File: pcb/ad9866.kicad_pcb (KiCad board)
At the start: 4 copper layers, 48.8 x 51 mm, 71 parts, among them CN1 MEC6-140_CONNECTOR_BEMICRO, CN2 PCIE, P1 CONN_4, P10 CONN_1, P13 CONN_1, P14 CONN_1, P15 Si510 73.728, P16 CONN_3X2, P17 CONN_4, P18 CONN_1, P19 CONN_1, P2 CONN_1, P20 CONN_1, P22 CONN_1, P23 CONN_5, P24 CONN_5, P25 CONN_5, P3 CONN_1, P4 CONN_1, P5 CONN_1, P6 CONN_1, P8 CONN_1, P9 CONN_1, T1 TRANSF_ADT8, T2 TRANSF_ADT2, T3 TRANSF_ADT2, U1 AD9866BCPZ, U2 NCP1117ST33T3G, U3 NCP1117ST33T3G

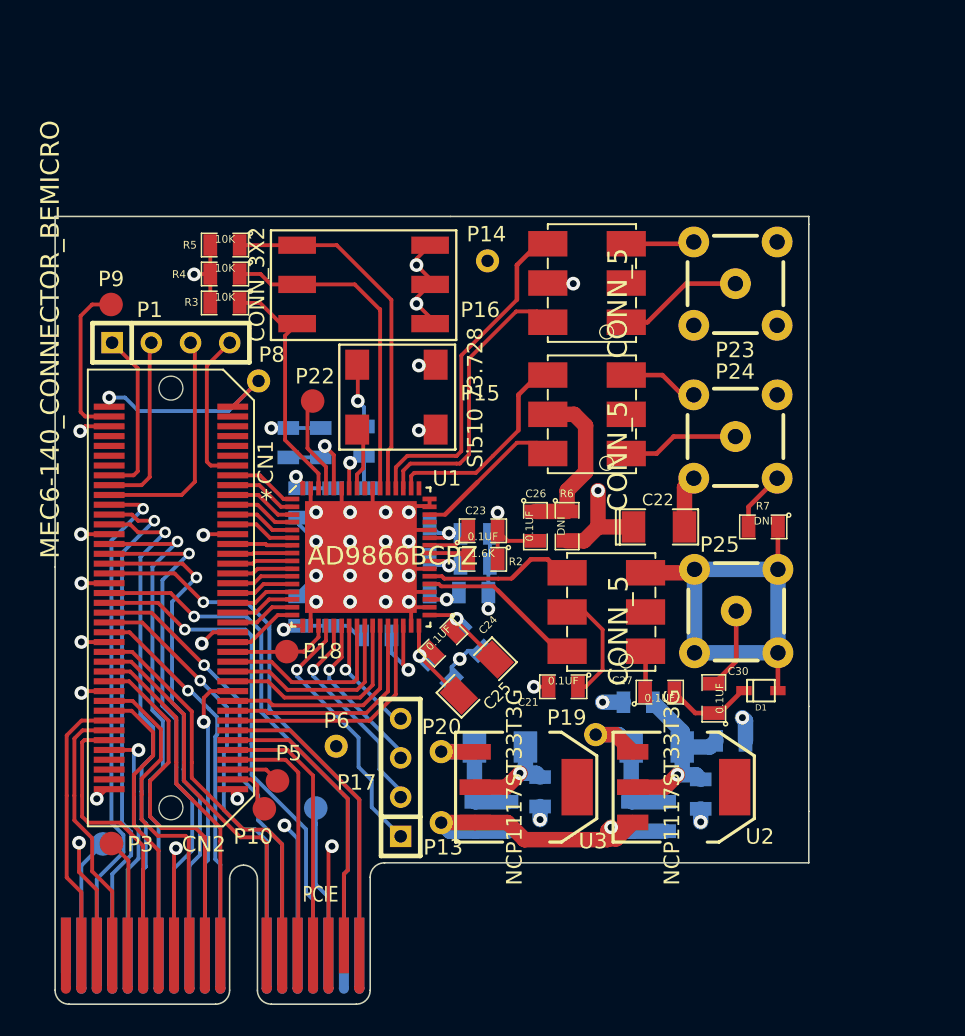
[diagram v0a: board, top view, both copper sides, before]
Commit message: Think 12 is fixed; routed by hand all changes.
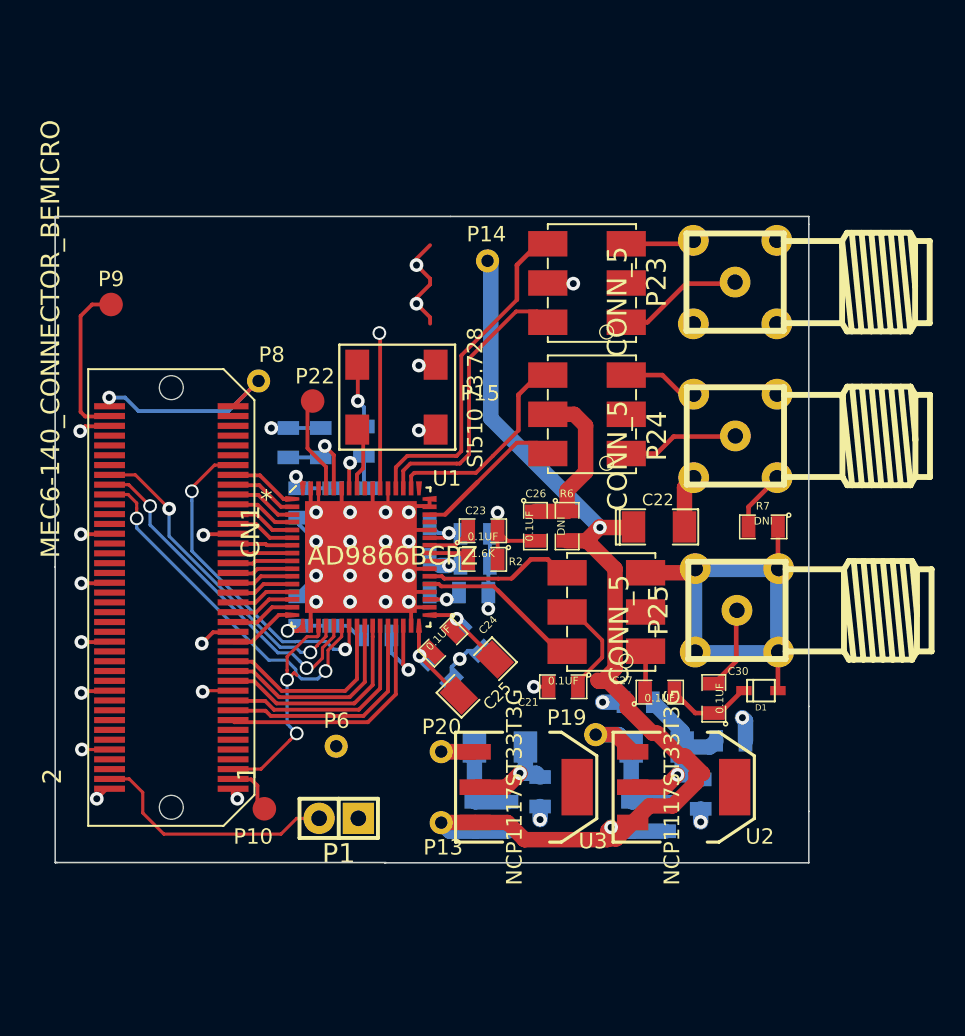
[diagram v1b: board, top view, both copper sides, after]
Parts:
- removed CN2: PCIE, Connect:PCI-EXPRESS
- removed P16: CONN_3X2, DIPSWITCH:DIPSWITCH
- removed P17: CONN_4, Connect:SIL-4
- removed P18, P2, P3, P4, P5: CONN_1, Measurement_Points:Measurement_Point_Round-SMD-Pad_Small
- removed R3, R4, R5: 10K, SMD_Packages:SM0805
- P1: value CONN_4 -> CONN_2; footprint Connect:SIL-4 -> Pin_Headers:Pin_Header_Straight_1x02
- P23, P24, P25: footprint BEMICRO:SMA -> SMA:SMA
- moved P1 32.7 mm to (119.1, 122.4), turned to 180 degrees
- moved P23 0.10 mm to (144.7, 87.7)
- moved P25 0.07 mm to (144.8, 109.0)
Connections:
- CN1 pad 11: Net-(CN1-Pad11) -> (no net)
- CN1 pad 12: Net-(CN1-Pad12) -> (no net)
- CN1 pad 13: Net-(CN1-Pad13) -> (no net)
- CN1 pad 14: Net-(CN1-Pad14) -> (no net)
- CN1 pad 16: Net-(CN1-Pad16) -> (no net)
- CN1 pad 18: Net-(CN1-Pad18) -> (no net)
- CN1 pad 20: Net-(CN1-Pad20) -> (no net)
- CN1 pad 24: Net-(CN1-Pad24) -> (no net)
- CN1 pad 26: Net-(CN1-Pad26) -> (no net)
- CN1 pad 28: Net-(CN1-Pad28) -> (no net)
- CN1 pad 29: Net-(CN1-Pad29) -> (no net)
- CN1 pad 30: Net-(CN1-Pad30) -> (no net)
- CN1 pad 34: Net-(CN1-Pad34) -> (no net)
- CN1 pad 36: Net-(CN1-Pad36) -> (no net)
- CN1 pad 38: Net-(CN1-Pad38) -> (no net)
- CN1 pad 40: Net-(CN1-Pad40) -> (no net)
- CN1 pad 42: Net-(CN1-Pad42) -> (no net)
- CN1 pad 46: Net-(CN1-Pad46) -> (no net)
- CN1 pad 48: Net-(CN1-Pad48) -> (no net)
- CN1 pad 5: Net-(CN1-Pad5) -> /CLKOUT1
- CN1 pad 50: Net-(CN1-Pad50) -> (no net)
- CN1 pad 52: Net-(CN1-Pad52) -> (no net)
- CN1 pad 56: Net-(CN1-Pad56) -> (no net)
- CN1 pad 58: Net-(CN1-Pad58) -> (no net)
- CN1 pad 6: Net-(CN1-Pad6) -> (no net)
- CN1 pad 60: Net-(CN1-Pad60) -> (no net)
- CN1 pad 62: Net-(CN1-Pad62) -> SCLK
- CN1 pad 64: Net-(CN1-Pad64) -> SDO
- CN1 pad 66: Net-(CN1-Pad66) -> SDIO
- CN1 pad 67: Net-(CN1-Pad67) -> SEN
- CN1 pad 68: Net-(CN1-Pad68) -> (no net)
- CN1 pad 69: Net-(CN1-Pad69) -> (no net)
- CN1 pad 7: Net-(CN1-Pad7) -> (no net)
- CN1 pad 70: Net-(CN1-Pad70) -> (no net)
- CN1 pad 71: Net-(CN1-Pad71) -> (no net)
- CN1 pad 72: Net-(CN1-Pad72) -> (no net)
- CN1 pad 73: Net-(CN1-Pad73) -> (no net)
- CN1 pad 74: Net-(CN1-Pad74) -> (no net)
- CN1 pad 75: Net-(CN1-Pad75) -> (no net)
- CN1 pad 77: Net-(CN1-Pad77) -> (no net)
- CN1 pad 8: Net-(CN1-Pad8) -> (no net)
- CN1 pad 9: Net-(CN1-Pad9) -> (no net)
- P1 pad 1: Net-(CN1-Pad66) -> GND
- P1 pad 2: Net-(CN1-Pad64) -> Net-(CN1-Pad4)
- U1 pad 19: Net-(CN1-Pad29) -> /CLKOUT1
- U1 pad 45: Net-(U1-Pad45) -> (no net)
- U1 pad 49: Net-(U1-Pad49) -> (no net)
- U1 pad 53: Net-(P16-Pad6) -> GND
- U1 pad 54: Net-(P16-Pad4) -> GND
- U1 pad 56: Net-(U1-Pad56) -> (no net)
- U1 pad 62: Net-(P16-Pad2) -> GND
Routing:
- net GND: track 281.2 -> 236.5 mm, vias 38 -> 34
- net VIN: track 29.4 -> 73.3 mm, vias 2 -> 3
- net Net-(CN1-Pad46): track 35.4 -> 0.00 mm, vias 1 -> 0
- net Net-(CN1-Pad42): track 34.2 -> 0.00 mm, vias 1 -> 0
- net Net-(CN1-Pad50): track 33.1 -> 0.00 mm, vias 1 -> 0
- net Net-(CN1-Pad60): track 33.0 -> 0.00 mm, vias 1 -> 0
- net Net-(CN1-Pad52): track 32.8 -> 0.00 mm, vias 1 -> 0
- net Net-(CN1-Pad58): track 32.7 -> 0.00 mm, vias 1 -> 0
- net Net-(CN1-Pad56): track 32.6 -> 0.00 mm, vias 1 -> 0
- net Net-(CN1-Pad40): track 32.4 -> 0.00 mm, vias 1 -> 0
- net Net-(CN1-Pad48): track 32.1 -> 0.00 mm, vias 1 -> 0
- net Net-(CN1-Pad38): track 28.3 -> 0.00 mm, vias 1 -> 0
- net Net-(CN1-Pad36): track 27.5 -> 0.00 mm, vias 1 -> 0
- net Net-(CN1-Pad30): track 26.0 -> 0.00 mm
- net Net-(CN1-Pad34): track 24.7 -> 0.00 mm, vias 1 -> 0
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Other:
- board size 48.8 x 51 mm -> 48.8 x 41.8 mm
- net class Default: clearance 0.205 -> 0.155; trace_width 0.25 -> 0.205
- rule trace_clearance: 0.205 -> 0.155
- rule trace_min: 0.2 -> 0.155
- board text added: "SDR Rev 1.0 Copyright 2014 SofterHardware"
- board text removed: "SDR Rev 0.9 Copyright 2014 SofterHardware"

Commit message: Just making sure everything is saved.
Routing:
- net GND: track 236.5 -> 232.4 mm, vias 34 -> 33
- added copper zone on F.Cu, net GND
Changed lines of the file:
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@@
     (thickness 1.6)
     (drawings 15)
-    (tracks 657)
+    (tracks 658)
     (zones 0)
     (modules 60)
@@
   )
   (setup
-    (last_trace_width 1)
+    (last_trace_width 0.205)
     (user_trace_width 0.205)
     (user_trace_width 0.25)
@@
   (segment (start 124.98 90.39) (end 124.98 89.98) (width 0.25) (layer F.Cu) (net 0))
   (segment (start 124.1 88.73) (end 124.98 87.85) (width 0.25) (layer F.Cu) (net 0))
+  (segment (start 121.7446 91.0496) (end 121.695 91) (width 0.25) (layer F.Cu) (net 0))
   (segment (start 125.6157 106.05) (end 125.4025 106.05) (width 0.2) (layer B.Cu) (net 1))
   (segment (start 125.6157 106.05) (end 126.2 106.05) (width 1) (layer B.Cu) (net 1))
@@
   (segment (start 116.5 100.5) (end 116.5 101.0475) (width 0.254) (layer B.Cu) (net 4))
   (segment (start 116.5 109.9525) (end 118.7 109.9525) (width 0.254) (layer B.Cu) (net 4))
+  (segment (start 121.7446 101.055) (end 121.7446 104.2554) (width 0.205) (layer F.Cu) (net 5))
+  (segment (start 121.7446 104.2554) (end 120.5 105.5) (width 0.205) (layer F.Cu) (net 5))
+  (segment (start 121.262 101.055) (end 121.262 104.738) (width 0.205) (layer F.Cu) (net 5))
+  (segment (start 121.262 104.738) (end 120.5 105.5) (width 0.205) (layer F.Cu) (net 5))
   (segment (start 122.2526 101.055) (end 122.2526 103.7474) (width 0.205) (layer F.Cu) (net 5))
   (segment (start 122.2526 103.7474) (end 120.5 105.5) (width 0.205) (layer F.Cu) (net 5))
@@
   (via (at 102.435 117.96) (size 0.889) (layers F.Cu B.Cu) (net 5))
   (segment (start 102.4375 117.9625) (end 102.435 117.96) (width 0.205) (layer F.Cu) (net 5))
-  (segment (start 121.7446 91.0496) (end 121.695 91) (width 0.25) (layer F.Cu) (net 5))
-  (segment (start 121.7446 101.055) (end 121.7446 91.0496) (width 0.25) (layer F.Cu) (net 5))
-  (via (at 121.695 91) (size 0.889) (drill 0.635) (layers F.Cu B.Cu) (net 5))
   (segment (start 112.225 114.1525) (end 110.3225 114.1525) (width 0.205) (layer F.Cu) (net 5))
   (segment (start 110.3225 114.1525) (end 110.255 114.22) (width 0.205) (layer F.Cu) (net 5))
@@
   (segment (start 119.2554 101.055) (end 119.2554 104.2554) (width 0.25) (layer F.Cu) (net 5))
   (segment (start 119.2554 104.2554) (end 120.5 105.5) (width 0.25) (layer F.Cu) (net 5))
-  (segment (start 121.262 101.055) (end 121.262 104.738) (width 0.25) (layer F.Cu) (net 5))
   (segment (start 121.262 104.738) (end 120.5 105.5) (width 0.25) (layer F.Cu) (net 5))
   (segment (start 124.945 106.262) (end 121.262 106.262) (width 0.25) (layer F.Cu) (net 5))
@@
       )
     )
+  )
+  (zone (net 5) (net_name GND) (layer F.Cu) (hatch edge 0.508)
+    (connect_pads (clearance 0.45))
+    (min_thickness 0.254)
+    (fill yes (arc_segments 16) (thermal_gap 0.5) (thermal_bridge_width 0.26))
+    (polygon
+      (pts
+        (xy 148.9 124.7) (xy 129.2 124.7) (xy 129.2 115.9) (xy 124.2 110.9) (xy 123.2 111.5)
+        (xy 128.2 116.5) (xy 128.2 124.7) (xy 101.325 124.7) (xy 101.325 84.05) (xy 117.8 84.05)
+        (xy 117.8 99) (xy 118.8 99) (xy 118.8 84.05) (xy 148.9 84.05)
+      )
+    )

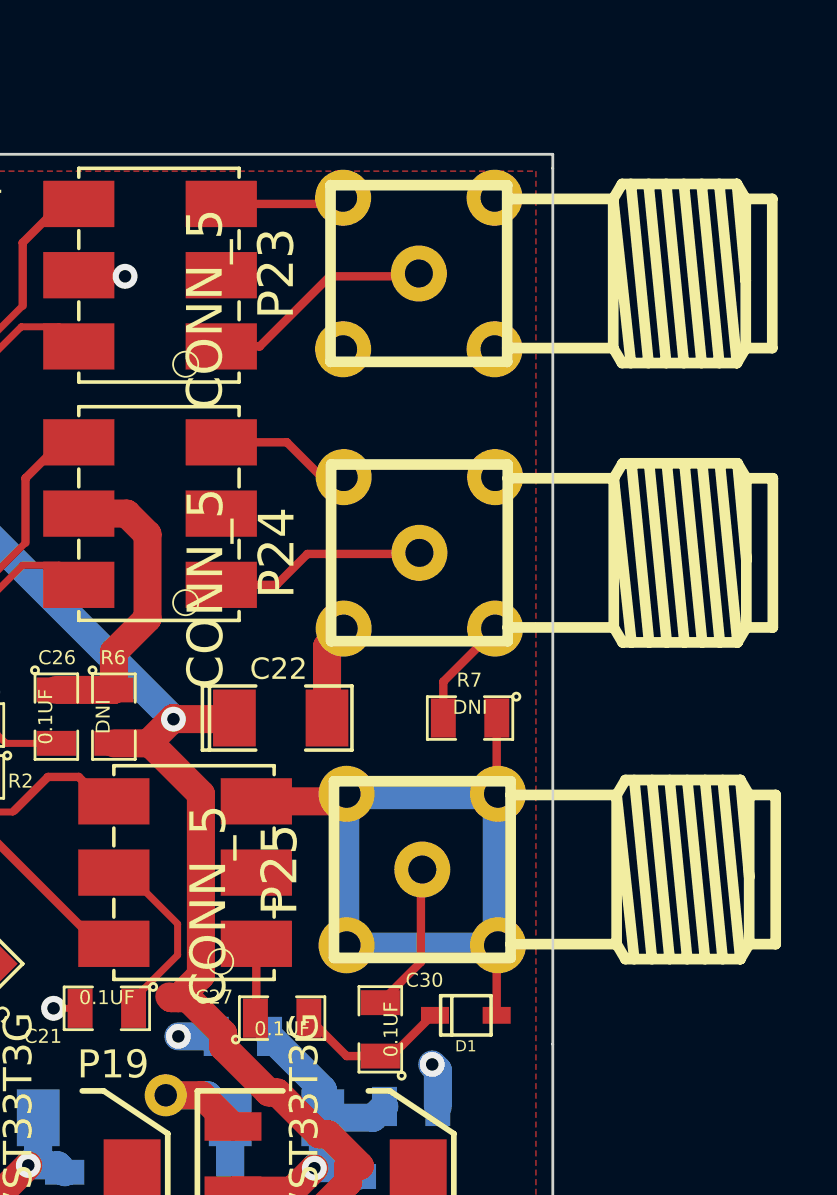
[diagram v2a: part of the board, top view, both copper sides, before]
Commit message: Changed the SMA to SMA edge connectors, because then they are the same as the other board, and to get around the slight possibility the holes still are not right.
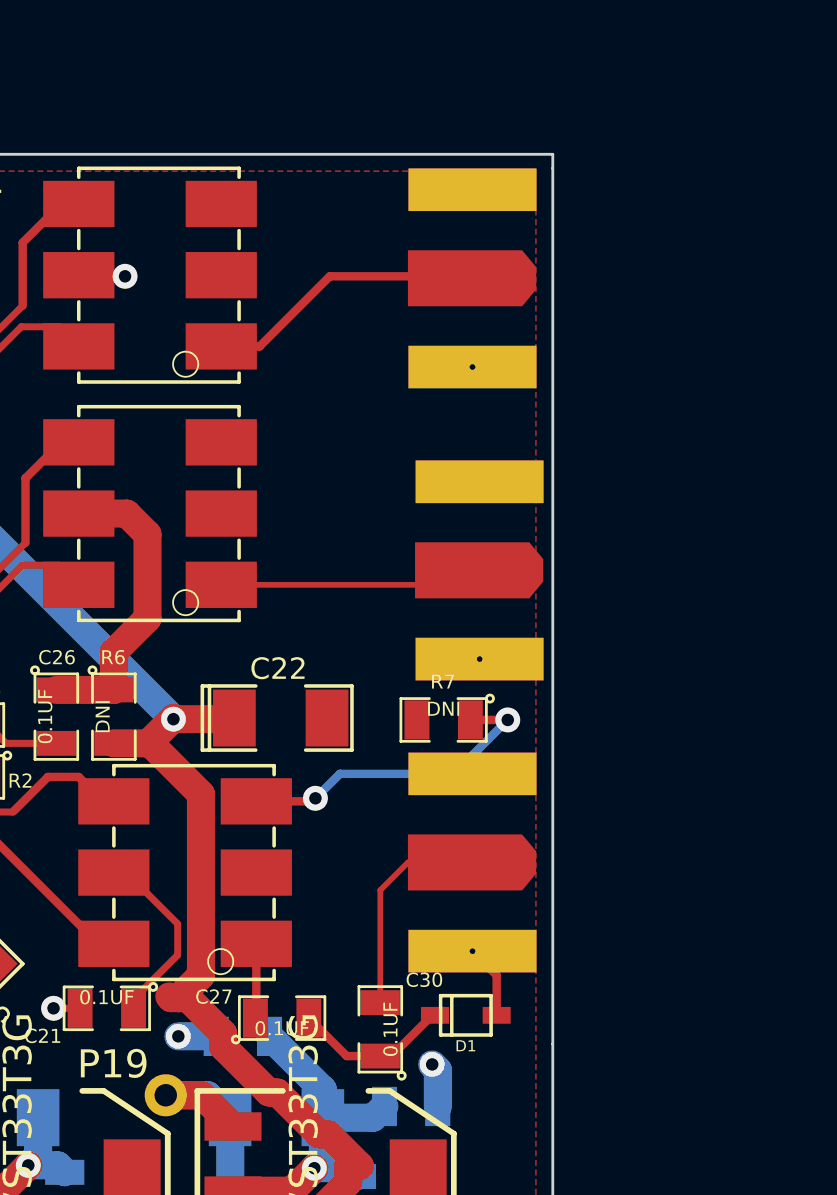
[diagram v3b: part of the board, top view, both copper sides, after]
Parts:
- P23, P24, P25: value CONN_5 -> CONN_2; footprint SMA:SMA -> SMA_EDGE:SMA_EDGE; moved to B.Cu
- moved P24 11.2 mm to (155.8, 99.6), turned to 0 degrees
- moved P23 10.9 mm to (155.5, 89.1), turned to 0 degrees
- moved P25 10.7 mm to (155.5, 110.0), turned to 0 degrees
- moved R7 0.94 mm to (145.6, 103.6)
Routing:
- net GND: track 232.4 -> 215.8 mm
- net Net-(D1-Pad1): track 30.1 -> 14.6 mm, vias 0 -> 2
- net Net-(C30-Pad2): track 5.30 -> 9.73 mm
- net Net-(P24-Pad1): track 7.53 -> 11.4 mm
- net Net-(P23-Pad1): track 8.11 -> 11.9 mm
